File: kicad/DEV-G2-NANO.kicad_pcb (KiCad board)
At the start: 6 copper layers, 76.2 x 20.3 mm, 10 parts, among them U1 MAYA-W166-00B, U3 MIMXRT1171DVMAB

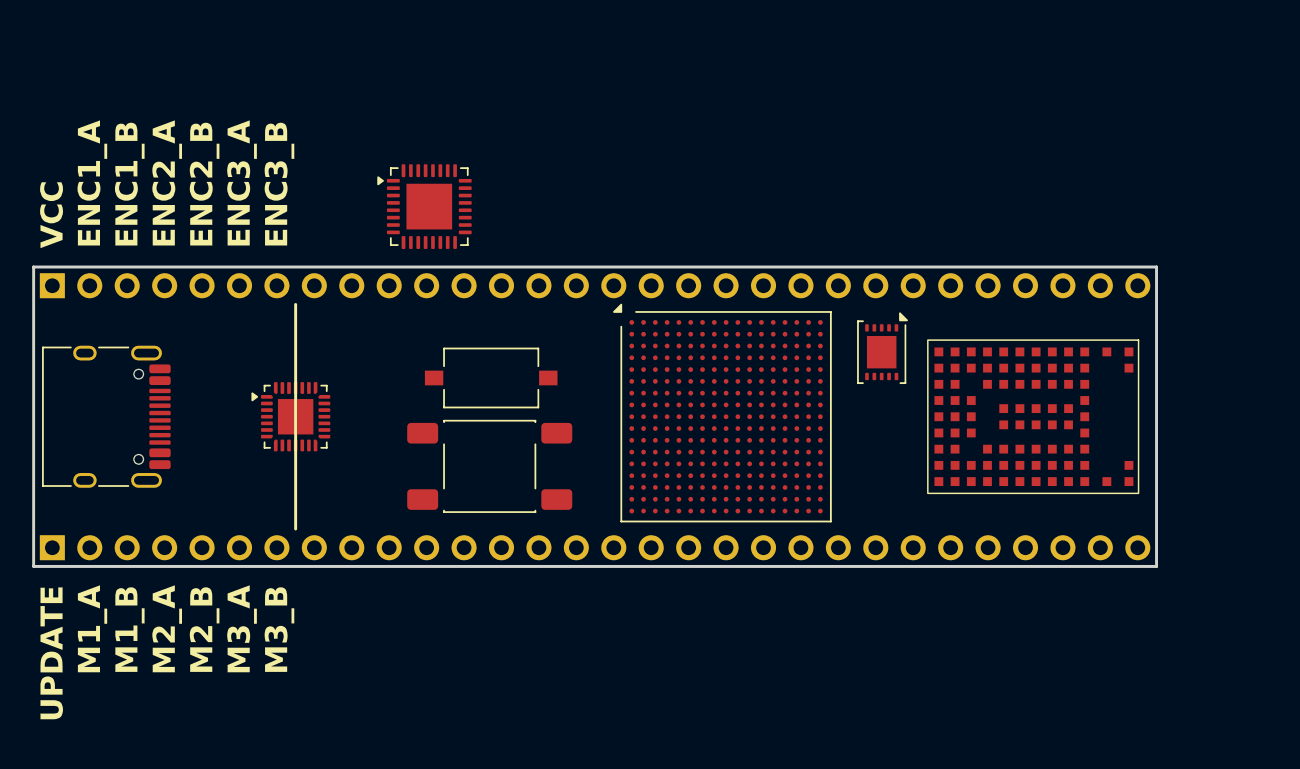
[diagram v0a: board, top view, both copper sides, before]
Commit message: added several footprints
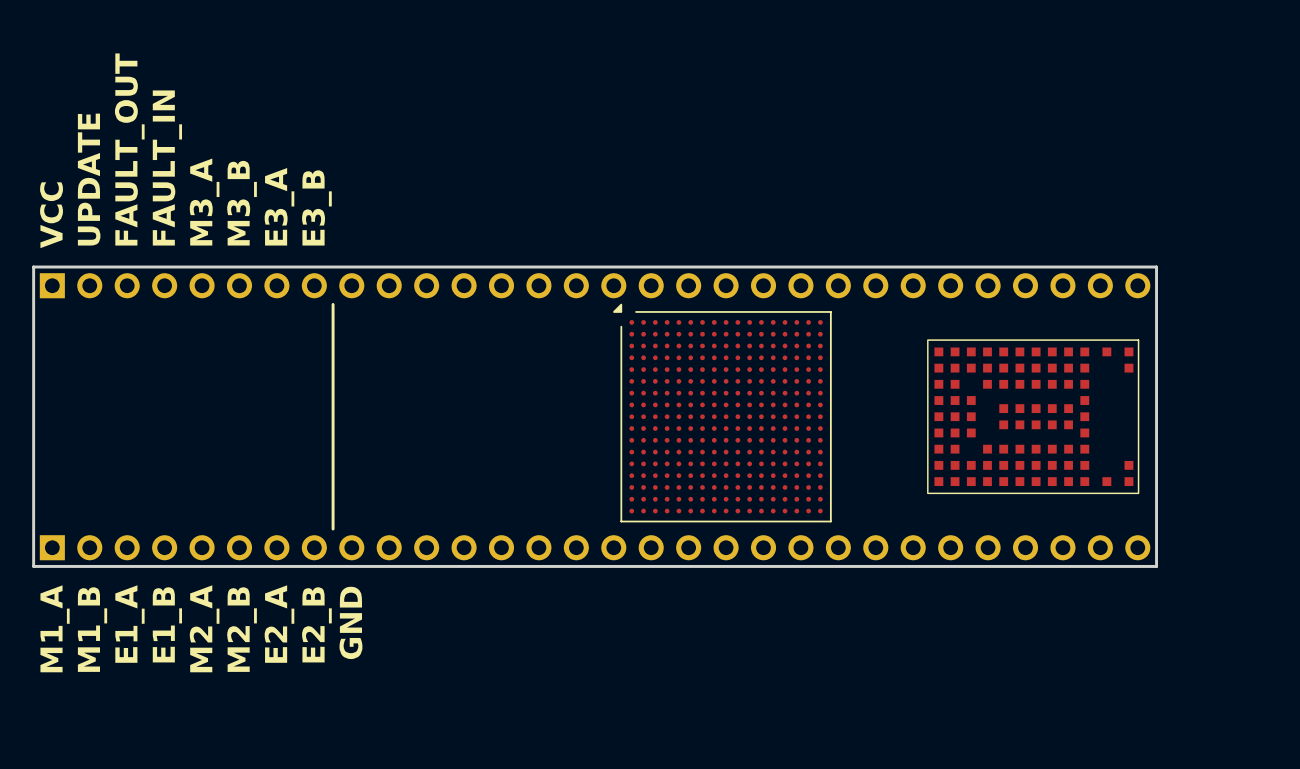
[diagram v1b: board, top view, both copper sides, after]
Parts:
- removed the REF** at (139.0, 97.7)
- removed the REF** at (138.9, 103.7)
- removed the REF** at (165.5, 96.0)
- removed the REF** at (112.5, 100.3)
- removed the REF** at (125.7, 100.3)
- removed the REF** at (134.8, 86.1)
- renumbered U3 to U1, U1 to U2
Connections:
- net Net-(U3A-DCDC_PSWITCH) renamed RC_DELAY
- U1 pad P5: unconnected-(U3B-GPIO_LPSR_09-PadP5) -> Net-(U1B-GPIO_LPSR_09)
- U1 pad P6: unconnected-(U3B-GPIO_LPSR_02-PadP6) -> Net-(U1B-GPIO_LPSR_02)
- U1 pad T10: unconnected-(U3B-POR_B-PadT10) -> Net-(U1B-POR_B)
- U1 pad T6: unconnected-(U3B-GPIO_LPSR_14-PadT6) -> Net-(U1B-GPIO_LPSR_14)
- U1 pad T7: unconnected-(U3B-GPIO_LPSR_03-PadT7) -> Net-(U1B-GPIO_LPSR_03)
- U1 pad U7: unconnected-(U3B-GPIO_LPSR_15-PadU7) -> Net-(U1B-GPIO_LPSR_15)
- U1 pad U8: unconnected-(U3B-GPIO_LPSR_08-PadU8) -> Net-(U1B-GPIO_LPSR_08)
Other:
- board text added: "E1_A"
- board text added: "E1_B"
- board text added: "E2_A"
- board text added: "E2_B"
- board text added: "E3_A"
- board text added: "E3_B"
- board text added: "FAULT_IN"
- board text added: "FAULT_OUT"
- board text added: "GND"
- board text removed: "ENC1_A"
- board text removed: "ENC1_B"
- board text removed: "ENC2_A"
- board text removed: "ENC2_B"
- board text removed: "ENC3_A"
- board text removed: "ENC3_B"

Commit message: finished preliminary layout
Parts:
- removed REF** (x2): PinHeader_1x30_P2.54mm_Vertical, Connector_PinHeader_2.54mm:PinHeader_1x30_P2.54mm_Vertical
- added C45: 100nF, Capacitor_SMD:C_0201_0603Metric, B.Cu at (159.0, 97.7)
- added C46: 4.7μF, Capacitor_SMD:C_0402_1005Metric, B.Cu at (159.0, 98.5)
- added C48: 4.7μF, Capacitor_SMD:C_0402_1005Metric, B.Cu at (165.0, 100.5)
- added C49: 1μF, Capacitor_SMD:C_0201_0603Metric, B.Cu at (166.2, 95.2)
- added C50: 2.2μF, Capacitor_SMD:C_0201_0603Metric, B.Cu at (159.8, 92.8)
- added C51: 4.7μF, Capacitor_SMD:C_0402_1005Metric, B.Cu at (161.5, 92.8)
- added C52: 2.2μF, Capacitor_SMD:C_0201_0603Metric, B.Cu at (165.4, 97.7)
- added C57: 100nF, Capacitor_SMD:C_0201_0603Metric, B.Cu at (160.2, 97.2)
- added C58: 2.2μF, Capacitor_SMD:C_0201_0603Metric, B.Cu at (161.4, 97.7)
- added C59: 1μF, Capacitor_SMD:C_0201_0603Metric, B.Cu at (164.2, 97.2)
- added C60: 1μF, Capacitor_SMD:C_0201_0603Metric, B.Cu at (167.4, 96.5)
- added C63: 100nF, Capacitor_SMD:C_0201_0603Metric, B.Cu at (161.0, 96.5)
- added C64: 2.2μF, Capacitor_SMD:C_0201_0603Metric, B.Cu at (161.8, 96.5)
- added C66: 100nF, Capacitor_SMD:C_0201_0603Metric, B.Cu at (161.8, 94.0)
- added C67: 1μF, Capacitor_SMD:C_0201_0603Metric, B.Cu at (163.8, 94.5)
- added C68: 1μF, Capacitor_SMD:C_0201_0603Metric, B.Cu at (161.4, 95.2)
- added C69: 4.7μF, Capacitor_SMD:C_0402_1005Metric, B.Cu at (163.8, 95.3)
- added C70: 4.7μF, Capacitor_SMD:C_0402_1005Metric, B.Cu at (163.0, 97.0)
- added C78: 2.2μF, Capacitor_SMD:C_0201_0603Metric, B.Cu at (166.6, 90.8)
- added C79: 2.2μF, Capacitor_SMD:C_0201_0603Metric, B.Cu at (165.8, 93.2)
- added C80: 2.2μF, Capacitor_SMD:C_0201_0603Metric, B.Cu at (160.6, 94.5)
- added C81: 4.7μF, Capacitor_SMD:C_0402_1005Metric, B.Cu at (159.7, 95.3)
- added C82: 2.2μF, Capacitor_SMD:C_0201_0603Metric, B.Cu at (165.0, 90.8)
- added C83: 2.2μF, Capacitor_SMD:C_0201_0603Metric, B.Cu at (161.0, 91.7)
- added C84: 2.2μF, Capacitor_SMD:C_0201_0603Metric, B.Cu at (161.0, 99.7)
- added C85: 2.2μF, Capacitor_SMD:C_0201_0603Metric, B.Cu at (167.8, 93.7)
- added C86: 10μF, Capacitor_SMD:C_0402_1005Metric, B.Cu at (128.1, 90.2)
- added C87: 22μF, Capacitor_SMD:C_0603_1608Metric, F.Cu at (132.1, 91.0)
- added C89: 4.7μF, Capacitor_SMD:C_0402_1005Metric, B.Cu at (129.7, 100.0)
- added C90: 22μF, Capacitor_SMD:C_0603_1608Metric, F.Cu at (133.3, 99.2)
- added D1: RED, LED_SMD:LED_0603_1608Metric, F.Cu at (147.3, 90.2)
- added D2: BAT54C, project_footprints:BAT54C, B.Cu at (152.4, 100.3)
- added D3: RED, LED_SMD:LED_0603_1608Metric, F.Cu at (123.4, 100.1)
- added J2: Lower Bank, project_footprints:Header-1x30, B.Cu at (116.8, 104.1)
- added J3: Upper Bank, project_footprints:Header-1x30, B.Cu at (190.5, 86.4)
- added J4: USB C, project_footprints:UJ20-C-H-G-SMT-5-P16, F.Cu at (118.1, 95.2)
- added J5: HIC SWD, project_footprints:TestPoints-3, B.Cu at (127.0, 95.2)
- added J6: RTC Battery, project_footprints:Header-1x02, F.Cu at (148.6, 100.3)
- added L1: 10μH, Inductor_SMD:L_1008_2520Metric, B.Cu at (147.3, 96.9)
- added L2: 4.7μH, project_footprints:SDCL1V4018, F.Cu at (152.7, 100.3)
- added L3: 470nH, project_footprints:L_0806, F.Cu at (130.2, 91.0)
- added L4: 470nH, project_footprints:L_0806, F.Cu at (131.5, 99.2)
- added R13: 5.1kΩ, Resistor_SMD:R_0201_0603Metric, B.Cu at (122.3, 94.0)
- added R16: 5.1kΩ, Resistor_SMD:R_0201_0603Metric, B.Cu at (122.3, 97.0)
- added SW1: PTS815, project_footprints:PTS815, F.Cu at (147.3, 95.2)
- added U10: TPS62086, project_footprints:TPS62086, F.Cu at (127.7, 90.2)
- added U11: TPS62825, project_footprints:TPS62825, F.Cu at (129.2, 100.0)
- added U4: LSM6DSV, project_footprints:LSM6DSV, F.Cu at (152.7, 90.2)
- added U5: LIS2MDL, project_footprints:LIS2MDL, F.Cu at (152.7, 94.0)
- added U6: RTMC-G2-4IQ48, project_footprints:RTMC-G2-4IQ48, B.Cu at (139.7, 95.2)
- added U7: W25Q64JWUUIQ, project_footprints:W25Q64JWUUIQ, F.Cu at (172.7, 92.7)
- added U8: MKL26Z128VFM4, project_footprints:MKL26Z128VFM4, F.Cu at (127.0, 95.2)
- added U9: LM66200, project_footprints:LM66200, F.Cu at (124.5, 90.2)
- added Y1: 8MHz, project_footprints:Crystal-4-Pin, B.Cu at (147.3, 91.9)
- added Y2: 16MHz, project_footprints:Crystal-4-Pin, F.Cu at (132.1, 95.2)
- added Y3: 24MHz, project_footprints:Crystal-4-Pin, F.Cu at (172.7, 100.3)
- added Y4: 32.768kHz, project_footprints:Crystal-2-Pin, F.Cu at (172.7, 96.8)
- U2: renamed from U1; footprint Package_BGA:MAPBGA-289_14x14mm_Layout17x17_P0.8mm -> project_footprints:MIMXRT1171DVMAB
- moved U2 9.16 mm to (162.6, 95.2)
- moved U3 9.16 mm to (183.6, 95.2)
- renumbered U2 to U3
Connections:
- U2 pad D17: Net-(J1-Pin_1) -> +5V
- U2 pad G12: +3V3 -> Net-(U2A-VDD_USB_3P3)
- U2 pad G16: V_{DCDC_ANA} -> +1V8
- U2 pad H12: V_{DCDC_ANA} -> Net-(U2A-VDD_USB_1P8)
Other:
- board text added: "+"
- board text added: "-"
- board text added: "G2 Nano"
- board text added: "VIN (+5V)"
- board text removed: "E1_A"
- board text removed: "E1_B"
- board text removed: "E2_A"
- board text removed: "E2_B"
- board text removed: "E3_A"
- board text removed: "E3_B"
- board text removed: "FAULT_IN"
- board text removed: "FAULT_OUT"
- board text removed: "M1_A"
- board text removed: "M1_B"
- board text removed: "M2_A"
- board text removed: "M2_B"
- board text removed: "M3_A"
- board text removed: "M3_B"
- board text removed: "UPDATE"
- board text removed: "VCC"

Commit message: removed USB host and 1.8V DAC
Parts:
- renumbered C45 to C43, C46 to C44, C48 to C46, C49 to C47, C50 to C48, C51 to C49, C52 to C50, C57 to C55, C58 to C56, C59 to C57, C60 to C58, C63 to C61, C64 to C62, C66 to C64, C67 to C65, C68 to C66, C69 to C67, C70 to C68, C78 to C76, C79 to C77, C80 to C78, C81 to C79, C82 to C80, C83 to C81, C84 to C82, C85 to C83, C86 to C84, C87 to C85, C89 to C87, C90 to C88, J4 to J3, J5 to J4, J6 to J5, U2 to U1, U11 to U10, U3 to U2, U4 to U3, U5 to U4, U6 to U5, U7 to U6, U8 to U7, U9 to U8, U10 to U9
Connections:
- U1 pad D17: +5V -> (no net)
- U1 pad E16: Net-(J1-Pin_2) -> (no net)
- U1 pad E17: Net-(J1-Pin_3) -> (no net)
- U1 pad H16: unconnected-(U2C-DAC_OUT-PadH16) -> (no net)

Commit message: set PCB design rules
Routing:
- removed copper zone on In4.Cu, net +3V3
- removed copper zone on In1.Cu, net GND
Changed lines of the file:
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@@
 	(generator_version "10.0")
 	(general
-		(thickness 1.6)
+		(thickness 1.5584)
 		(legacy_teardrops no)
 	)
@@
 		(10 "In4.Cu" power "PWR.Cu")
 		(2 "B.Cu" signal)
-		(9 "F.Adhes" user "F.Adhesive")
-		(11 "B.Adhes" user "B.Adhesive")
 		(13 "F.Paste" user)
 		(15 "B.Paste" user)
@@
 		(1 "F.Mask" user)
 		(3 "B.Mask" user)
-		(17 "Dwgs.User" user "User.Drawings")
-		(19 "Cmts.User" user "User.Comments")
-		(21 "Eco1.User" user "User.Eco1")
-		(23 "Eco2.User" user "User.Eco2")
 		(25 "Edge.Cuts" user)
 		(27 "Margin" user)
@@
 		(35 "F.Fab" user)
 		(33 "B.Fab" user)
-		(39 "User.1" user)
-		(41 "User.2" user)
-		(43 "User.3" user)
-		(45 "User.4" user)
 	)
 	(setup
@@
 			(layer "dielectric 1"
 				(type "prepreg")
-				(thickness 0.1)
+				(thickness 0.0994)
 				(material "FR4")
 				(epsilon_r 4.5)
@@
 			(layer "In1.Cu"
 				(type "copper")
-				(thickness 0.035)
+				(thickness 0.0152)
 			)
 			(layer "dielectric 2"
 				(type "core")
-				(thickness 0.535)
+				(thickness 0.55)
 				(material "FR4")
 				(epsilon_r 4.5)
@@
 			(layer "In2.Cu"
 				(type "copper")
-				(thickness 0.035)
+				(thickness 0.0152)
 			)
 			(layer "dielectric 3"
 				(type "prepreg")
-				(thickness 0.1)
+				(thickness 0.1088)
 				(material "FR4")
 				(epsilon_r 4.5)
@@
 			(layer "In3.Cu"
 				(type "copper")
-				(thickness 0.035)
+				(thickness 0.0152)
 			)
 			(layer "dielectric 4"
 				(type "core")
-				(thickness 0.535)
+				(thickness 0.55)
 				(material "FR4")
 				(epsilon_r 4.5)
@@
 			(layer "In4.Cu"
 				(type "copper")
-				(thickness 0.035)
+				(thickness 0.0152)
 			)
 			(layer "dielectric 5"
 				(type "prepreg")
-				(thickness 0.1)
+				(thickness 0.0994)
 				(material "FR4")
 				(epsilon_r 4.5)
@@
 		(capping no)
 		(filling no)
+		(zone_defaults)
 		(pcbplotparams
 			(layerselection 0x00000000_00000000_55555555_5755f5ff)
@@
 		(duplicate_pad_numbers_are_jumpers no)
 		(fp_rect
-			(start -5.2 -6.95)
-			(end 5.2 7.35)
+			(start -5.4 -7.15)
+			(end 5.4 7.55)
 			(stroke
 				(width 0.1)
@@
 			(layer "F.CrtYd")
 		)
+		(fp_rect
+			(start -5.2 -6.95)
+			(end 5.2 7.35)
+			(stroke
+				(width 0.1)
+				(type solid)
+			)
+			(fill no)
+			(layer "F.Fab")
+		)
 		(pad "A1" smd rect
 			(at 4.4 6.6 270)
@@
 		)
 	)
-	(zone
-		(net "GND")
-		(layer "In1.Cu")
-		(hatch edge 0.5)
-		(connect_pads
-			(clearance 0.5)
-		)
-		(min_thickness 0.25)
-		(fill yes
-			(thermal_gap 0.5)
-			(thermal_bridge_width 0.5)
-			(island_removal_mode 0)
-		)
-		(polygon
-			(pts
-				(xy 107.95 90.17) (xy 107.95 110.49) (xy 184.15 110.49) (xy 184.15 90.17)
-			)
-		)
-	)
-	(zone
-		(net "+3V3")
-		(layer "In4.Cu")
-		(hatch edge 0.5)
-		(connect_pads
-			(clearance 0.5)
-		)
-		(min_thickness 0.25)
-		(fill yes
-			(thermal_gap 0.5)
-			(thermal_bridge_width 0.5)
-			(island_removal_mode 0)
-		)
-		(polygon
-			(pts
-				(xy 107.95 90.17) (xy 107.95 110.49) (xy 184.15 110.49) (xy 184.15 90.17)
-			)
-		)
-	)
